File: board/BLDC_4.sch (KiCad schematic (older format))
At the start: 8 parts, among them P4 IN+, P5 IN-, P6 MOTOR1, P7 MOTOR2, P9 MOTOR3

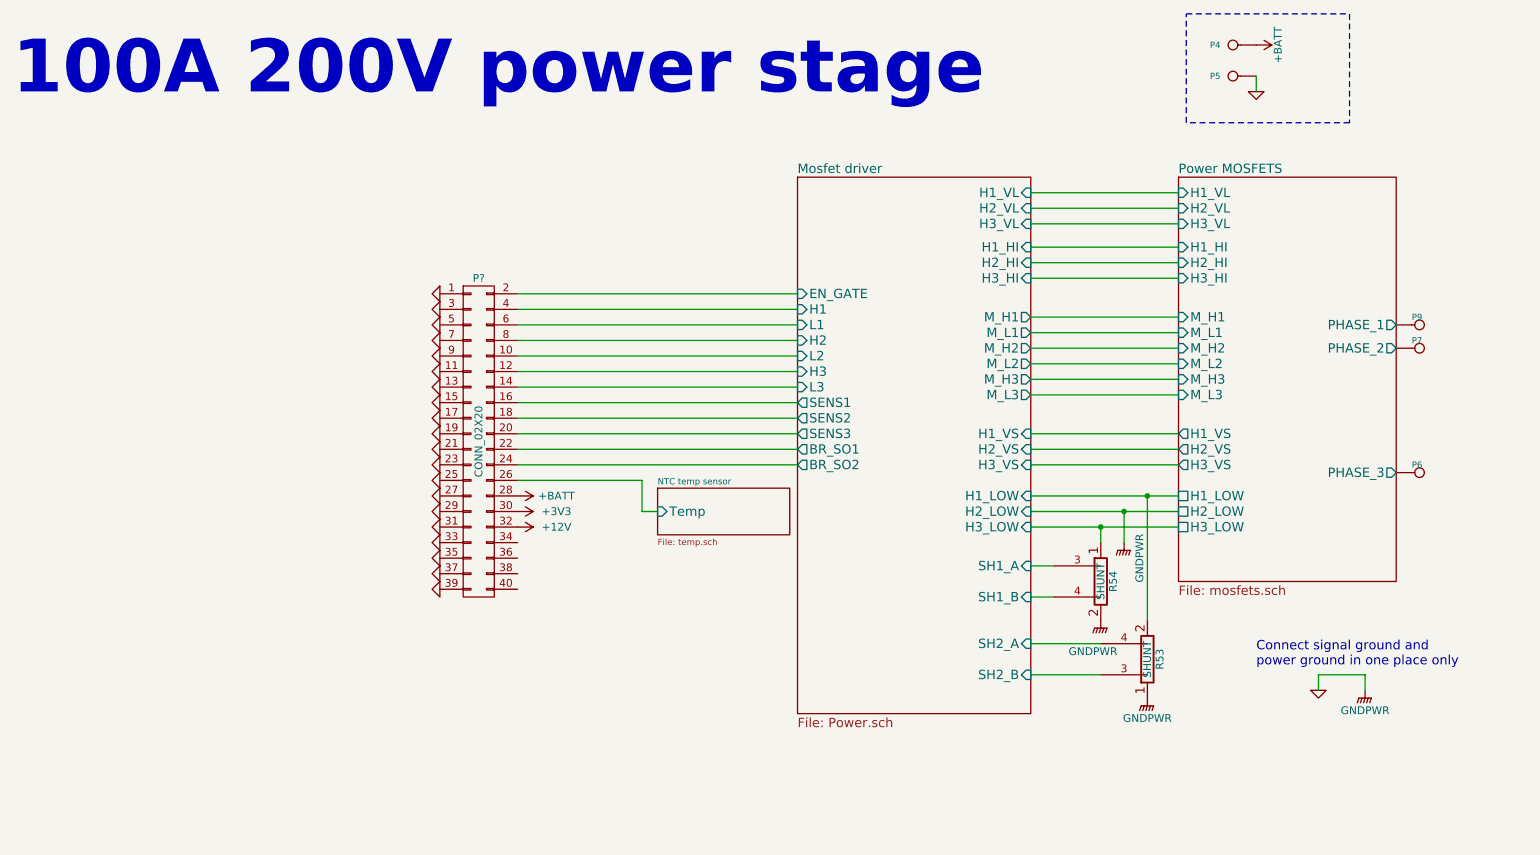
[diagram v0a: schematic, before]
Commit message: - implemented complementary transistor package - started layout
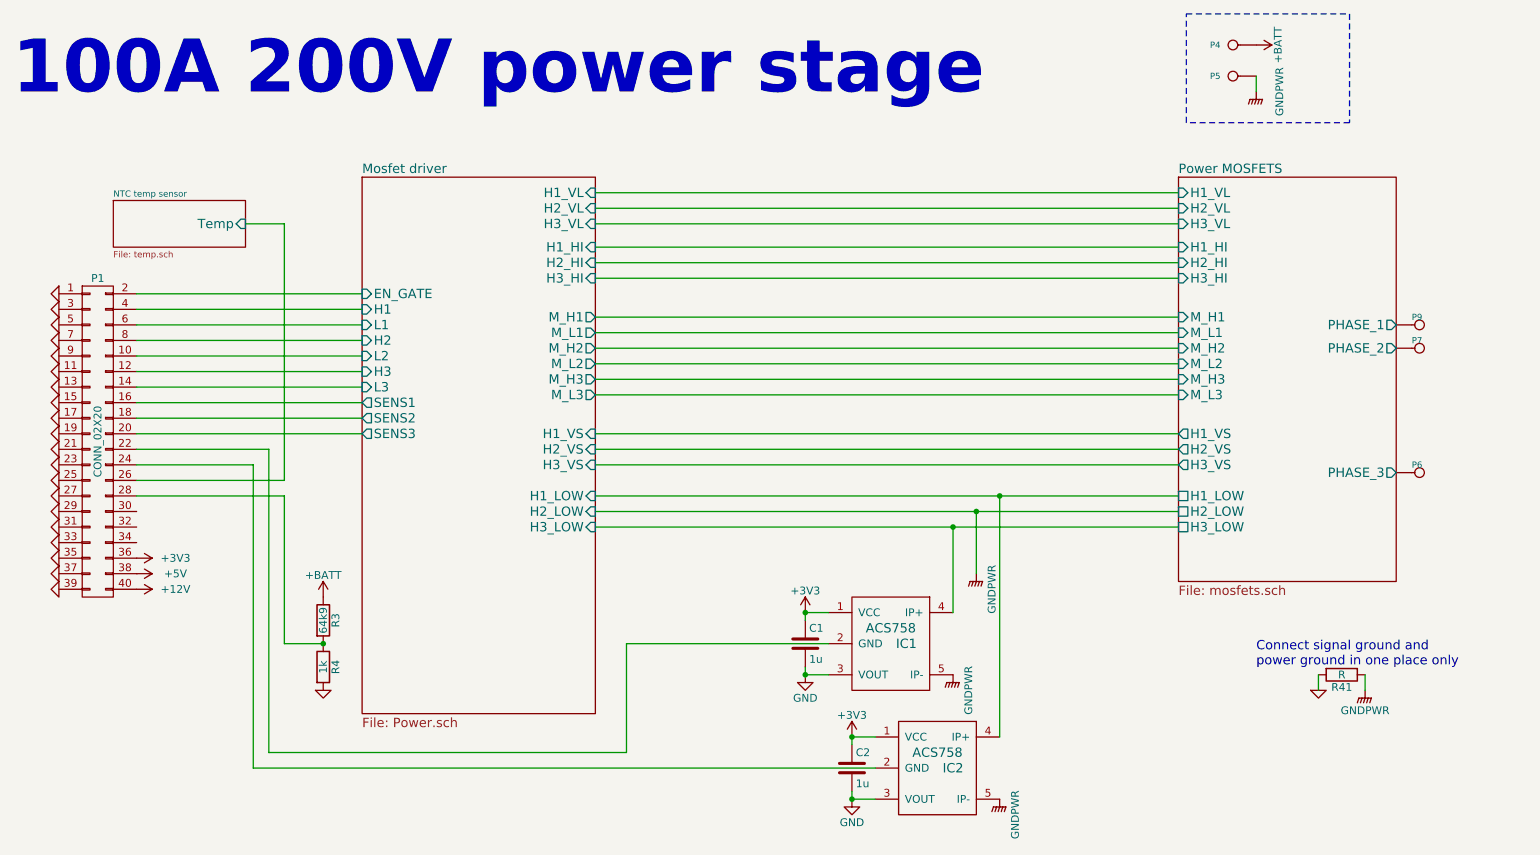
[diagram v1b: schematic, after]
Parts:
- removed R53, R54: SHUNT, CRF1:WSLP2726, symbol SHUNT
- added C1, C2: 1u, Capacitors_SMD:C_0805, symbol C
- added IC1, IC2: ACS758, alexmod:CB-PFF, symbol ACS758
- added R3: 64k9, Resistors_SMD:R_0805, symbol R
- added R4: 1k, Resistors_SMD:R_0805, symbol R
- added R41: R, Resistors_SMD:R_0805, symbol R
- P1: renamed from P?; footprint (none) -> alexmod:XG4A_40
- P4, P5, P6, P7, P9: footprint CRF1:1PAD_4x5mm -> Mounting_Holes:MountingHole_6.5mm_Pad_Via
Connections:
- net +12V: now also P1.40 (P40); no longer P1.32 (P32)
- net +3V3: now also P1.36 (P36), C1.1, C2.1, IC1.1 (VCC), IC2.1 (VCC); no longer P1.30 (P30)
- net +BATT: now also R3.1; no longer P1.28 (P28)
- net GND: now also C1.2, C2.2, IC1.3 (VOUT), IC2.3 (VOUT), R4.2, R41.2; no longer P5.1
- net Mosfet driver/H1_LOW: now also IC2.4 (IP+)
- net Mosfet driver/H3_LOW: now also IC1.4 (IP+)
- net +5V: now reaches P1.38 (P38)
- net Mosfet driver/BR_SO1: no longer names the net of P1.22 (P22)
- net Mosfet driver/BR_SO1: now also IC1.2 (GND)
- net Mosfet driver/BR_SO2: no longer names the net of P1.24 (P24)
- net Mosfet driver/BR_SO2: now also IC2.2 (GND)
- new net: P1.28 (P28), R3.2, R4.1
- new net GNDPWR: IC1.5 (IP-), IC2.5 (IP-), P5.1, R41.1
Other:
- moved on the sheet: P1
